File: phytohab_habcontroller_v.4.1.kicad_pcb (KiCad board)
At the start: 4 copper layers, 150 x 70 mm, 109 parts, among them J1 UMPT-02-01-L-RA-WT-M-TR, J10 I²C, J11 I²C, J12 I²C, J13 I²C, J14 I²C, J2 Micro_SD_Card, J3 DF40HC_3.0_-100DS-0.4V_58, J4 DF40HC_3.0_-100DS-0.4V_58, J523 GPIO, J525 PWM 4, J526 PWM 3, J527 PWM 2, J528 PWM 1, J7 I²C, J8 I²C, J847 GPIO, J848 GPIO, J849 GPIO, J850 GPIO, J851 GPIO, J852 GPIO, J853 GPIO, J9 I²C, U101 DMP3037LSS-13, U301 MIC37100-3.3WS-TR, U501 DS3231M+TRL, U601 PCA9548ARGE, U701 PCF8575DBR, U801 PCA9685BS, U802 PCA9685BS

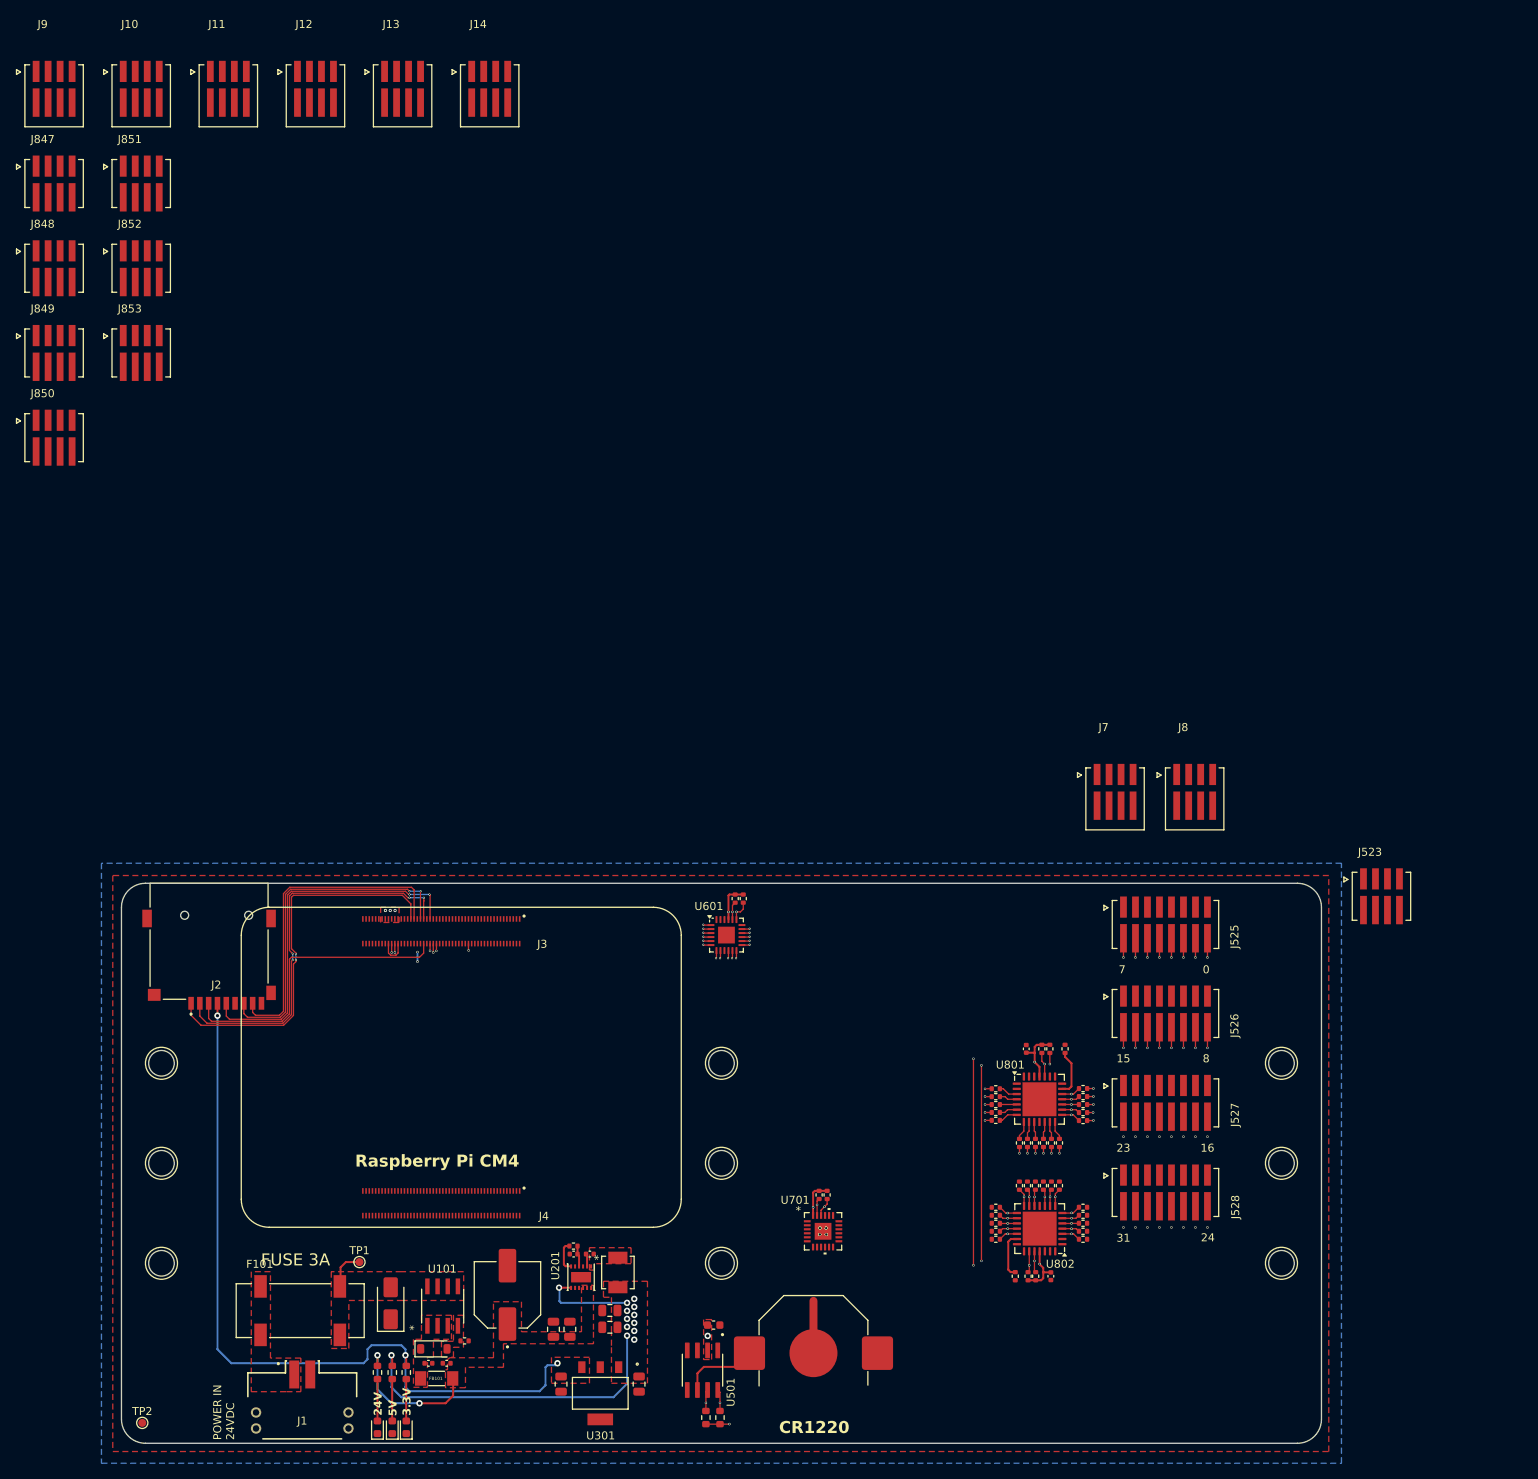
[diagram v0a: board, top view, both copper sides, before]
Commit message: Add files via upload
cleaned up, board outline changed, cons cleaned up, 
GPIO now prepped for breakout board.
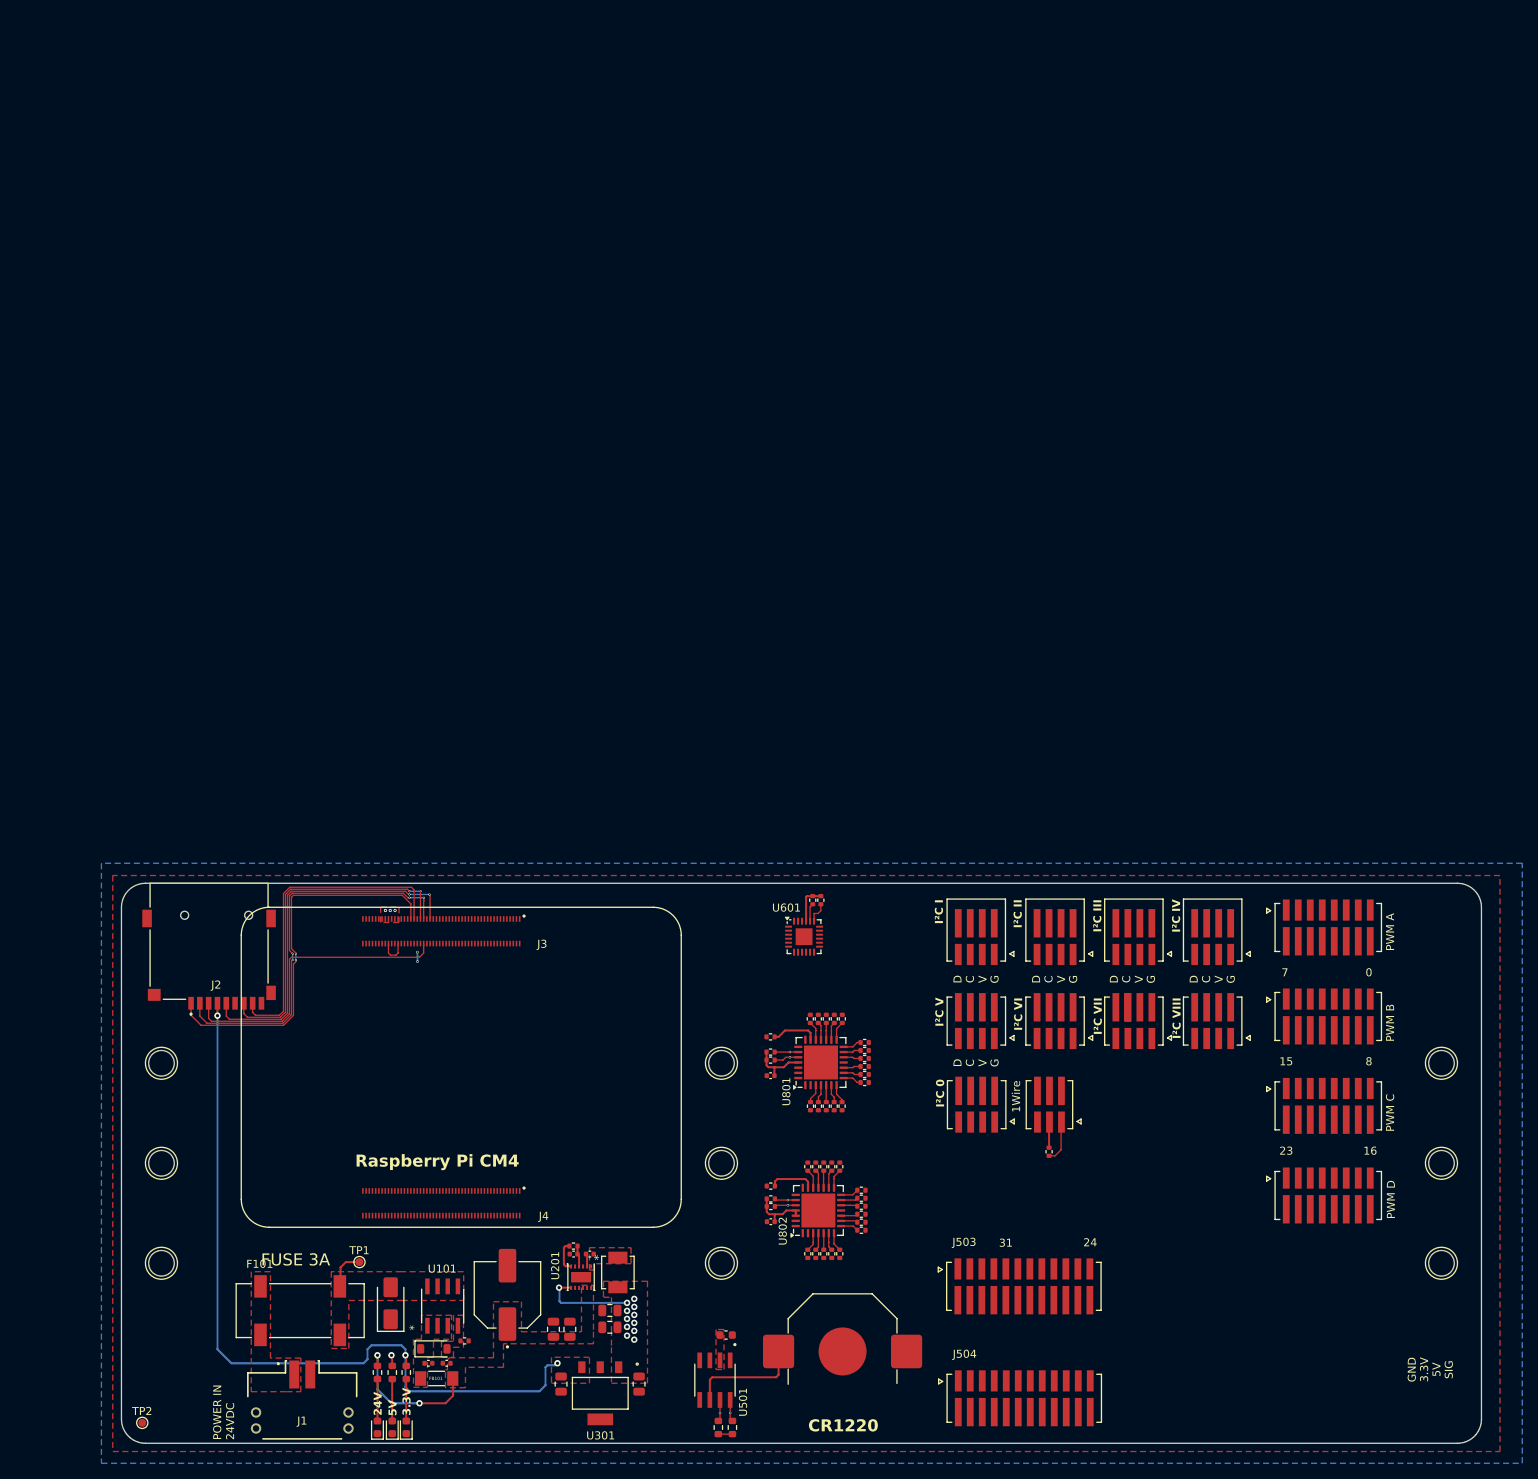
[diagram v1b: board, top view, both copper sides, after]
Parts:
- removed J523, J847, J848, J849, J850, J851, J852, J853: GPIO, connectors_molex:MOLEX_874370443
- removed R701, R702: 10k, Resistor_SMD:R_0402_1005Metric
- removed U701: PCF8575DBR, PFC8575CRGER:RGE24_2P1X2P1
- added ?: , , F.Cu at (160.8, 50.5)
- added J501: I²C, connectors_molex:MOLEX_874370443, F.Cu at (141.9, 62.7)
- added J502: Molex_PicoSPOX_87437_3pos, connectors_molex:MOLEX_874370343, F.Cu at (151.0, 62.7)
- added J503: Molex_PicoSPOX_87438_12pos, connectors_molex:MOLEX_874371243, F.Cu at (147.8, 85.4)
- added J504: Molex_PicoSPOX_87438_12pos, connectors_molex:MOLEX_874371243, F.Cu at (147.8, 99.4)
- added R1001: 4,7k, Resistor_SMD:R_0402_1005Metric, F.Cu at (150.9, 68.6)
- J11, J12, J13, J14: footprint connectors_molex:Molex_PicoSpox_hor_4pos_874380443 -> connectors_molex:MOLEX_874370443
- moved J9 170.6 mm to (161.6, 40.9), turned to 180 degrees
- moved J10 169.7 mm to (171.4, 40.9), turned to 180 degrees
- moved J11 148.7 mm to (141.9, 52.2), turned to 180 degrees
- moved J12 148.1 mm to (151.7, 52.2), turned to 180 degrees
- moved J13 147.4 mm to (161.6, 52.2), turned to 180 degrees
- moved J14 146.8 mm to (171.4, 52.2), turned to 180 degrees
- moved R803 36.8 mm to (116.1, 54.2), turned to 0 degrees
- moved C802 35.7 mm to (116.2, 77.3), turned to 0 degrees
- moved R836 35.2 mm to (121.1, 52.0), turned to 90 degrees
- moved R801 34.9 mm to (116.1, 56.1), turned to 180 degrees
- moved R835 34.5 mm to (122.1, 52.0), turned to 90 degrees
- moved R841 34.5 mm to (120.8, 81.3), turned to -90 degrees
- moved R839 34.2 mm to (116.2, 75.4), turned to 180 degrees
- moved R802 33.9 mm to (116.1, 57.1), turned to 180 degrees
- moved R834 33.8 mm to (123.1, 52.0), turned to 90 degrees
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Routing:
- net SDA1 (GPIO2): track 128.2 -> 8.02 mm, vias 6 -> 2
- net SCL1 (GPIO3): track 128.4 -> 8.37 mm, vias 6 -> 2
- net SCL0: track 93.9 -> 2.74 mm, vias 2 -> 1
- net SDA0: track 93.2 -> 2.71 mm, vias 2 -> 1
- net PWM8: track 53.9 -> 0.00 mm, vias 2 -> 0
- net PWM0: track 51.7 -> 0.00 mm, vias 2 -> 0
- net PWM9: track 51.3 -> 0.00 mm, vias 2 -> 0
- net PWM1: track 50.2 -> 0.00 mm, vias 2 -> 0
- net PWM2: track 48.8 -> 0.00 mm, vias 2 -> 0
- net PWM10: track 48.5 -> 0.00 mm, vias 2 -> 0
- net PWM3: track 47.2 -> 0.00 mm, vias 2 -> 0
- net PWM4: track 45.5 -> 0.00 mm, vias 2 -> 0
- net PWM5: track 43.0 -> 0.00 mm, vias 2 -> 0
- net VSYS1: track 70.1 -> 28.9 mm, vias 20 -> 16
- net PWM6: track 40.5 -> 0.00 mm, vias 2 -> 0
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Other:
- board size 150 x 70 mm -> 170 x 70 mm
- board text added: "1Wire"
- board text added: "C"
- board text added: "D"
- board text added: "G"
- board text added: "GND"
- board text added: "I²C 0"
- board text added: "I²C I"
- board text added: "I²C II"
- board text added: "I²C III"
- board text added: "I²C IV"
- board text added: "I²C V"
- board text added: "I²C VI"
- board text added: "I²C VII"
- board text added: "I²C VIII"
- board text added: "PWM A"
- board text added: "PWM B"
- board text added: "PWM C"
- board text added: "PWM D"
- board text added: "SIG"
- board text added: "V"

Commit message: pcb changes
GPIO-cons routed (what a mess)
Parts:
- removed ?: , 
- moved J11 101.1 mm to (208.4, -23.9), turned to 0 degrees
- moved J12 86.7 mm to (208.4, -13.3), turned to 0 degrees
- moved J501 79.9 mm to (208.4, 18.5), turned to 0 degrees
- moved J13 72.2 mm to (208.4, -2.73), turned to 0 degrees
- moved J14 57.8 mm to (208.4, 7.87), turned to 0 degrees
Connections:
- J3 pad 24: GPIO 26 -> GPIO26
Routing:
- net GPIO25: track 0.00 -> 140.9 mm, vias 0 -> 4
- net GPIO24: track 0.00 -> 139.9 mm, vias 0 -> 4
- net GPIO23: track 0.00 -> 138.3 mm, vias 0 -> 4
- net GPIO15: track 0.00 -> 133.9 mm, vias 0 -> 4
- net GPIO27: track 0.00 -> 132.5 mm, vias 0 -> 4
- net GPIO22: track 0.00 -> 132.2 mm, vias 0 -> 4
- net GPIO18: track 0.00 -> 131.6 mm, vias 0 -> 4
- net GPIO14: track 0.00 -> 131.3 mm, vias 0 -> 2
- net GPIO21: track 0.00 -> 128.0 mm, vias 0 -> 4
- net GPIO26: track 0.00 -> 126.8 mm, vias 0 -> 4
- net GPIO20: track 0.00 -> 126.6 mm, vias 0 -> 4
- net GPIO16: track 0.00 -> 121.7 mm, vias 0 -> 2
- net GPIO12: track 0.00 -> 120.9 mm, vias 0 -> 4
- net GPIO8: track 0.00 -> 118.9 mm, vias 0 -> 4
- net GPIO17: track 0.00 -> 117.0 mm, vias 0 -> 4
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
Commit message: daughterboard created
divided into mainboard and daughterboard
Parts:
- removed C801, C802: 10uF, Capacitor_SMD:C_0402_1005Metric
- removed J502: Molex_PicoSPOX_87437_3pos, connectors_molex:MOLEX_874370343
- removed J503, J504: Molex_PicoSPOX_87438_12pos, connectors_molex:MOLEX_874371243
- removed J525: PWM 4, connectors_molex:MOLEX_874370863
- removed J526: PWM 3, connectors_molex:MOLEX_874370863
- removed J527: PWM 2, connectors_molex:MOLEX_874370863
- removed J528: PWM 1, connectors_molex:MOLEX_874370863
- removed R1001: 4,7k, Resistor_SMD:R_0402_1005Metric
- removed R801, R802, R803, R837, R839, R840: 10K, Resistor_SMD:R_0402_1005Metric
- removed R804, R806, R823, R824, R825, R826, R827, R828, R829, R830, R831, R832, R833, R834, R835, R836, R841, R842, R843, R844, R845, R846, R847, R848, R849, R850, R851, R852, R853, R854, R855, R856: 220, Resistor_SMD:R_0402_1005Metric
- removed U801, U802: PCA9685BS, Package_DFN_QFN:QFN-28-1EP_6x6mm_P0.65mm_EP4.25x4.25mm
- added TP3: TestPoint, TestPoint:TestPoint_Pad_D1.0mm, F.Cu at (39.9, 113.3)
- added TP4: TestPoint, TestPoint:TestPoint_Pad_D1.0mm, F.Cu at (104.7, 74.2)
- J11, J12, J13, J14: footprint connectors_molex:MOLEX_874370443 -> connectors_molex:MOLEX_874380443
- J15: renamed from J501; footprint connectors_molex:MOLEX_874370443 -> connectors_molex:MOLEX_874380443
- J7: footprint connectors_molex:Molex_PicoSpox_hor_4pos_874380443 -> connectors_molex:MOLEX_874380443
- moved DRA2 222.4 mm to (152.2, -148.4)
- moved DRA1 218.0 mm to (193.9, -147.9)
- moved J14 142.3 mm to (93.8, -76.5), turned to 180 degrees
- moved J13 128.1 mm to (103.7, -76.5), turned to 180 degrees
- moved J10 123.4 mm to (133.2, -76.5)
- moved J12 114.0 mm to (113.5, -76.5), turned to 180 degrees
- moved J9 108.2 mm to (144.4, -66.0), turned to 90 degrees
- moved J11 100.0 mm to (123.4, -76.5), turned to 180 degrees
- moved J8 97.3 mm to (144.4, -56.1), turned to 90 degrees
- moved U601 92.2 mm to (118.0, -50.5), turned to 180 degrees
- moved J7 87.2 mm to (144.4, -46.3), turned to 90 degrees
- moved J15 84.3 mm to (144.4, -36.5), turned to 90 degrees
- moved R601 83.2 mm to (116.5, -45.9), turned to 90 degrees
- moved R602 83.1 mm to (117.4, -45.9), turned to 90 degrees
- moved J2 66.3 mm to (51.8, 108.3), turned to 0 degrees
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- renumbered DRA501 to DRA1, DRA502 to DRA2, DRA503 to DRA3
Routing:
- net GPIO25: track 140.9 -> 0.00 mm, vias 4 -> 0
- net GPIO24: track 139.9 -> 0.00 mm, vias 4 -> 0
- net GPIO23: track 138.3 -> 0.00 mm, vias 4 -> 0
- net GPIO15: track 133.9 -> 0.00 mm, vias 4 -> 0
- net GPIO27: track 132.5 -> 0.00 mm, vias 4 -> 0
- net GPIO22: track 132.2 -> 0.00 mm, vias 4 -> 0
- net GPIO18: track 131.6 -> 0.00 mm, vias 4 -> 0
- net GPIO14: track 131.3 -> 0.00 mm, vias 2 -> 0
- net GPIO21: track 128.0 -> 0.00 mm, vias 4 -> 0
- net GPIO26: track 126.8 -> 0.00 mm, vias 4 -> 0
- net GPIO20: track 126.6 -> 0.00 mm, vias 4 -> 0
- net VSYS2: track 107.8 -> 232.3 mm, vias 4 -> 14
- net GPIO16: track 121.7 -> 0.00 mm, vias 2 -> 0
- net GPIO12: track 120.9 -> 0.00 mm, vias 4 -> 0
- net GPIO8: track 118.9 -> 0.00 mm, vias 4 -> 0
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- added copper zone on In2.Cu, net VSYS1
- removed copper zone on B.Cu, net VSYS1
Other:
- board size 170 x 70 mm -> 163 x 76 mm
- board text removed: "0"
- board text removed: "15"
- board text removed: "16"
- board text removed: "1Wire"
- board text removed: "23"
- board text removed: "24"
- board text removed: "31"
- board text removed: "7"
- board text removed: "8"
- board text removed: "PWM A"
- board text removed: "PWM B"
- board text removed: "PWM C"
- board text removed: "PWM D"

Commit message: CM4>RP3/4
changed SBC to RP3/4
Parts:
- removed J3, J4: DF40HC_3.0_-100DS-0.4V_58, connectors_Hirose:HRS_DF40HC_3.0_-100DS-0.4V_58
- added H3: MountingHole, MountingHole:MountingHole_2.7mm_M2.5_DIN965, F.Cu at (28.4, 82.5)
- added H4: MountingHole, MountingHole:MountingHole_2.7mm_M2.5_DIN965, F.Cu at (106.4, 82.5)
- added H5: MountingHole, MountingHole:MountingHole_2.7mm_M2.5_DIN965, F.Cu at (106.4, 33.5)
- J2: value Micro_SD_Card -> HTSS-120-01-L-DV; footprint MSD_4_A:CUI_MSD-4-A -> HTSS-120-01-L-DV:SAMTEC_HTSS-120-01-L-DV
- moved DRA2 214.9 mm to (118.0, 63.8)
- moved J10 106.8 mm to (155.5, 27.9)
- moved J11 106.8 mm to (145.7, 27.9)
- moved J12 106.8 mm to (135.8, 27.9)
- moved J13 106.8 mm to (126.0, 27.9)
- moved J14 106.8 mm to (116.1, 27.9)
- moved J9 95.9 mm to (165.3, 27.6), turned to 180 degrees
- moved U601 91.8 mm to (117.6, 41.3), turned to 90 degrees
- moved J8 89.5 mm to (175.2, 27.9), turned to 180 degrees
- moved R602 86.7 mm to (113.0, 40.7), turned to 0 degrees
- moved R601 85.7 mm to (113.0, 39.7), turned to 0 degrees
- moved J7 84.6 mm to (185.1, 27.9), turned to 180 degrees
- moved J15 81.8 mm to (194.9, 27.9), turned to 180 degrees
- moved J2 74.3 mm to (33.5, 36.3)
- moved FB101 54.3 mm to (58.0, 108.8), turned to 0 degrees
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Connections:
- R501 pad 2: SDA0 -> SCL0
- R502 pad 2: SCL0 -> SDA0
- R601 pad 2: SCL1 (GPIO3) -> SCL1
- R602 pad 2: SDA1 (GPIO2) -> SDA1
- U601 pad 19: SCL1 (GPIO3) -> SCL1
- U601 pad 20: SDA1 (GPIO2) -> SDA1
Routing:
- net VSYS2: track 232.3 -> 38.6 mm, vias 14 -> 15
- net SD_DAT3: track 78.6 -> 0.00 mm, vias 4 -> 0
- net SD_DAT2: track 77.5 -> 0.00 mm, vias 4 -> 0
- net SD_CMD: track 77.1 -> 0.00 mm, vias 2 -> 0
- net SD_CLK: track 76.4 -> 0.00 mm, vias 2 -> 0
- net SD_DAT0: track 76.2 -> 0.00 mm, vias 4 -> 0
- net SD_DAT1: track 74.8 -> 0.00 mm, vias 2 -> 0
- net SDA0: track 99.2 -> 82.6 mm, vias 5 -> 3
- net Net-(BT501-+): track 28.5 -> 18.6 mm, vias 2 -> 0
- net VSAFE: track 47.6 -> 39.8 mm, vias 2 -> 3
- net GPIO_VREF: track 5.00 -> 0.00 mm
- net Net-(U201-SW): track 0.00 -> 4.89 mm
- net Net-(D102-A): track 0.00 -> 4.61 mm
- net SCL0: track 99.8 -> 95.7 mm
- net SCL1 (GPIO3): track 2.32 -> 0.00 mm, vias 1 -> 0
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- added copper zone on B.Cu, net GND
- removed copper zone on F.Cu, net Net-(D102-A)
- removed copper zone on F.Cu, net Net-(U201-SW)
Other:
- board size 163 x 76 mm -> 180.9 x 89.8 mm
- board text removed: "Raspberry Pi CM4"
